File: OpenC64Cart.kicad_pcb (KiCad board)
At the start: 2 copper layers, 58.4 x 50.8 mm, 11 parts, among them P1 CONN_01X03, P2 CONN_01X02, P3 CONN_01X02, P4 CONN_01X03, P5 CONN_01X03, P6 CONN_01X03, SW1 RESET, U1 C64-Exp-Port, U2 27512

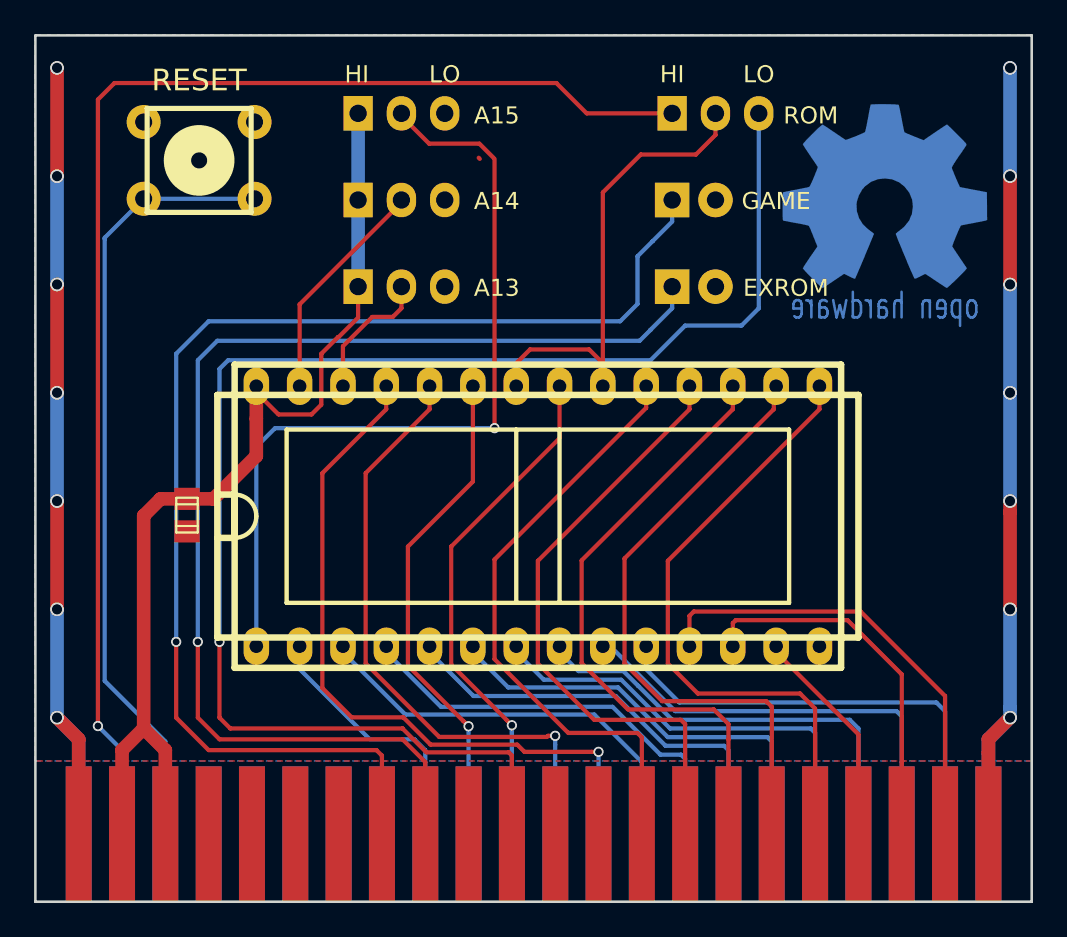
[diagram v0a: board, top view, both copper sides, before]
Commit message: Add peg hole, smooth corners and routing adjustments
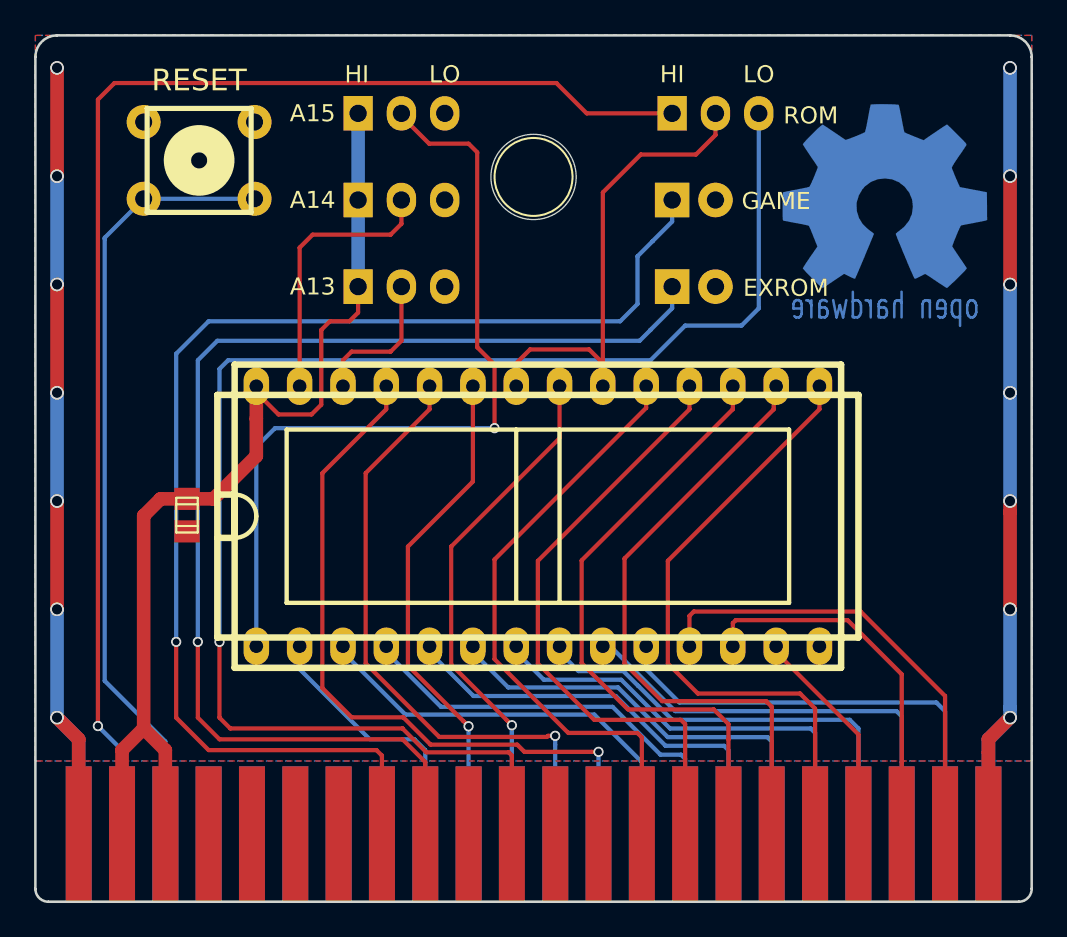
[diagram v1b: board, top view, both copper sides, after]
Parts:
- added REF**: PEG_HOLE, Connectors:1pin, F.Cu at (88.9, 87.0)
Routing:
- net Net-(P5-Pad2): track 13.4 -> 16.1 mm
- net +5V: track 61.0 -> 61.7 mm
- net Net-(P4-Pad2): track 7.97 -> 8.60 mm
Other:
- outline, holes or cut-outs redrawn
- rule pad_to_mask_clearance: 0.2 -> 0
- board text added: "V2"
- board text added: "github.com/SukkoPera/OpenC64Cart"
- board text removed: "V1.0"
- board text removed: "https://github.com/SukkoPera/OpenC64Cart"
